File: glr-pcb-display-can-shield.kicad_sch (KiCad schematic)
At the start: 11 parts, among them CN12 Conn_02x08_Odd_Even, CN6 Conn_01x08, CN8 Conn_01x06, IC1 L9615D013TR, IC2 LF80CDT-TR, J1 Screw_Terminal_01x04, J2 Screw_Terminal_01x08

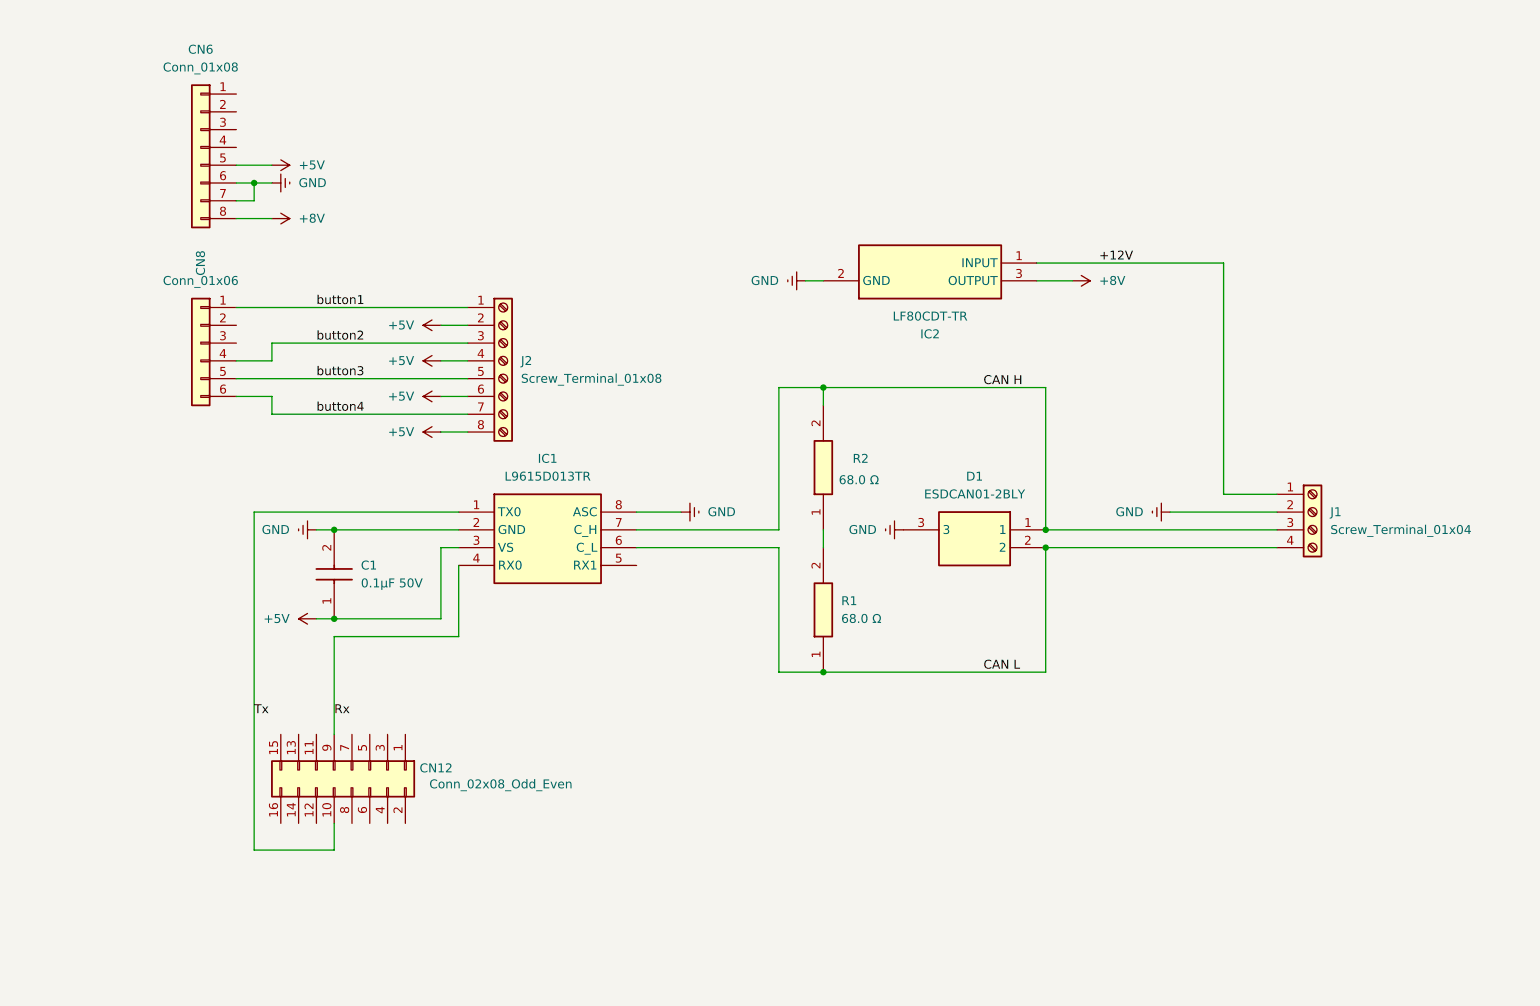
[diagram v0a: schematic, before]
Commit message: update can shield for new car
* provide more inputs for buttons and rotary encoders (not sure about that, big connector needed now)
* apply new can setup
* add new voltage transformer
* add full arduino headers
* m12a 4pin for power and can
* make board full size
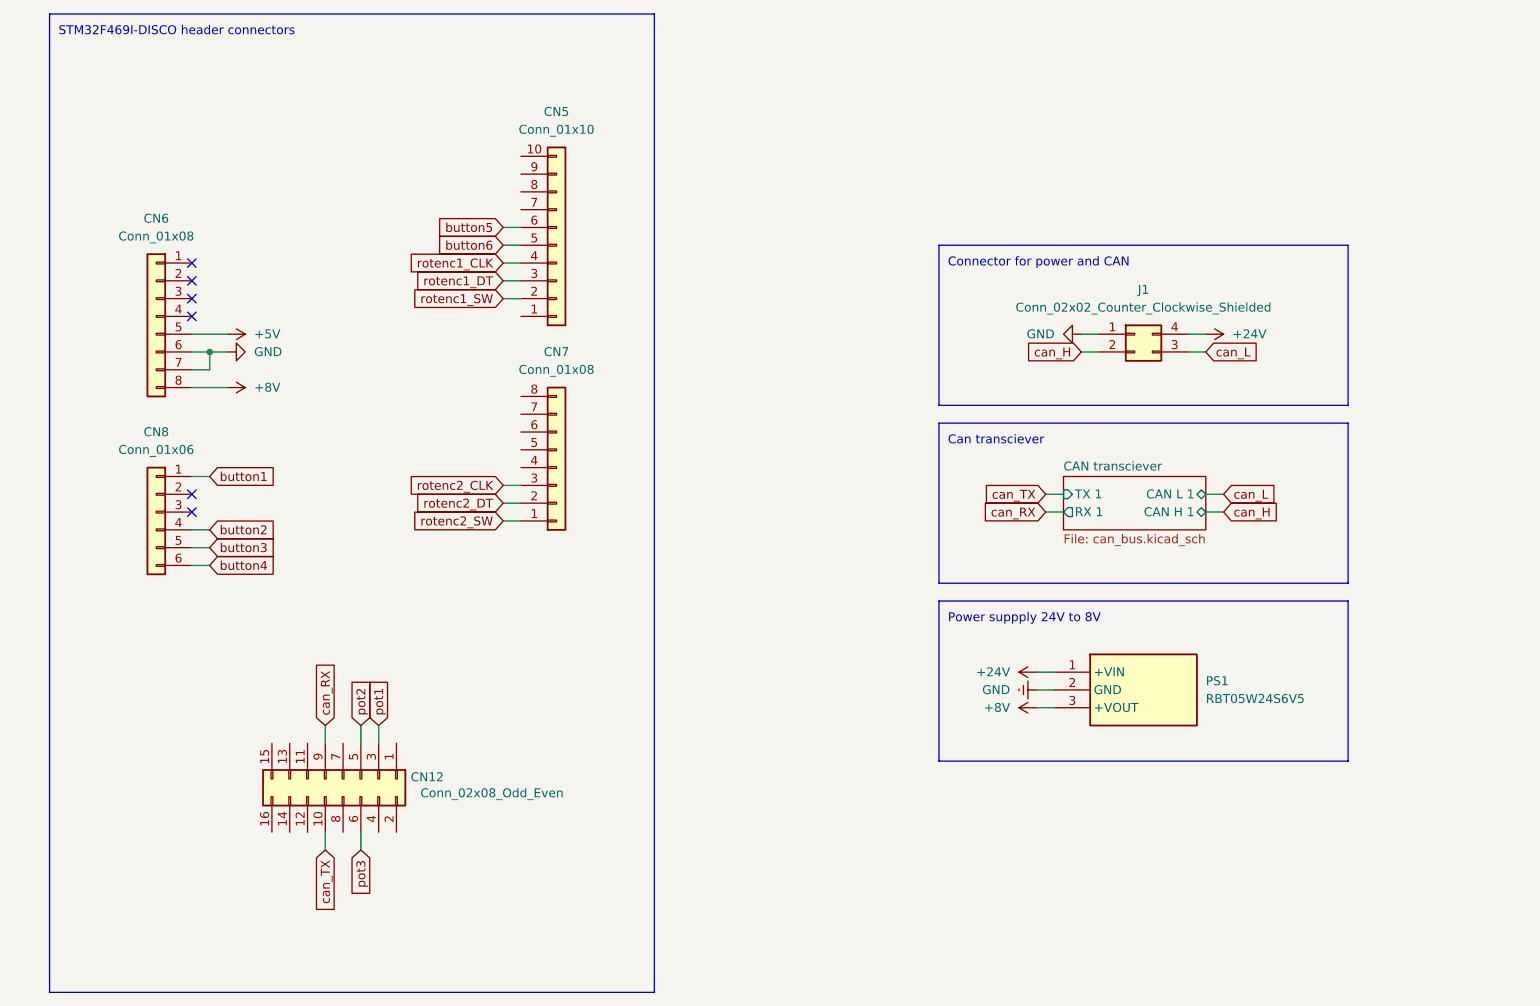
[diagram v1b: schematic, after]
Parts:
- removed C1: 0.1μF 50V, CAPC1608X90N, symbol SamacSys_Parts:CL10B104KB8NNNC
- removed D1: ESDCAN01-2BLY, SOT95P255X125-3N, symbol SamacSys_Parts:ESDCAN01-2BLY
- removed IC1: L9615D013TR, SOIC127P600X175-8N, symbol SamacSys_Parts:L9615D013TR
- removed IC2: LF80CDT-TR, LF80CDTTR, symbol SamacSys_Parts:LF80CDT-TR
- removed J1: Screw_Terminal_01x04, GLR_KiCAD_Library:WECO-950-FB-04, symbol Connector:Screw_Terminal_01x04
- removed J2: Screw_Terminal_01x08, GLR_KiCAD_Library:WECO-950-FB-08, symbol Connector:Screw_Terminal_01x08
- removed R1, R2: 68.0 Ω, RESC1608X50N, symbol SamacSys_Parts:CRCW060368R1FKEA
- added CN5: Conn_01x10, Connector_PinHeader_2.54mm:PinHeader_1x10_P2.54mm_Vertical, symbol Connector_Generic:Conn_01x10
- added CN7: Conn_01x08, Connector_PinHeader_2.54mm:PinHeader_1x08_P2.54mm_Vertical, symbol Connector_Generic:Conn_01x08
- added J1: Conn_02x02_Counter_Clockwise_Shielded, GLR_KiCad_Library:M12A-04P, symbol Connector_Generic:Conn_02x02_Counter_Clockwise
- added PS1: RBT05W24S6V5, RBT05W24S6V5, symbol SamacSys_Parts:RBT05W24S6V5
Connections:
- net +8V: now also PS1.3 (+VOUT)
- net GND: now also J1.1 (Pin_1), PS1.2 (GND)
- net pot1: now reaches CN12.3 (Pin_3)
- net pot2: now reaches CN12.5 (Pin_5)
- net pot3: now reaches CN12.6 (Pin_6)
- net Rx renamed can_RX
- net Tx renamed can_TX
- new net +24V: J1.4 (Pin_4), PS1.1 (+VIN)
- new net button5: CN5.6 (Pin_6)
- new net button6: CN5.5 (Pin_5)
- new net can_H: J1.2 (Pin_2)
- new net can_L: J1.3 (Pin_3)
- new net rotenc1_CLK: CN5.4 (Pin_4)
- new net rotenc1_DT: CN5.3 (Pin_3)
- new net rotenc1_SW: CN5.2 (Pin_2)
- new net rotenc2_CLK: CN7.3 (Pin_3)
- new net rotenc2_DT: CN7.2 (Pin_2)
- new net rotenc2_SW: CN7.1 (Pin_1)
- no-connect marks 0 -> 6
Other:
- added sheet CAN transciever (can_bus.kicad_sch)
- note added: "Can transciever"
- note added: "Connector for power and CAN"
- note added: "Power suppply 24V to 8V"
- note added: "STM32F469I-DISCO header connectors"
- moved on the sheet: CN12, CN6, CN8

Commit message: use absolute rotary encoders
* use more pins add dsub connector
* add documents
* routing should be done
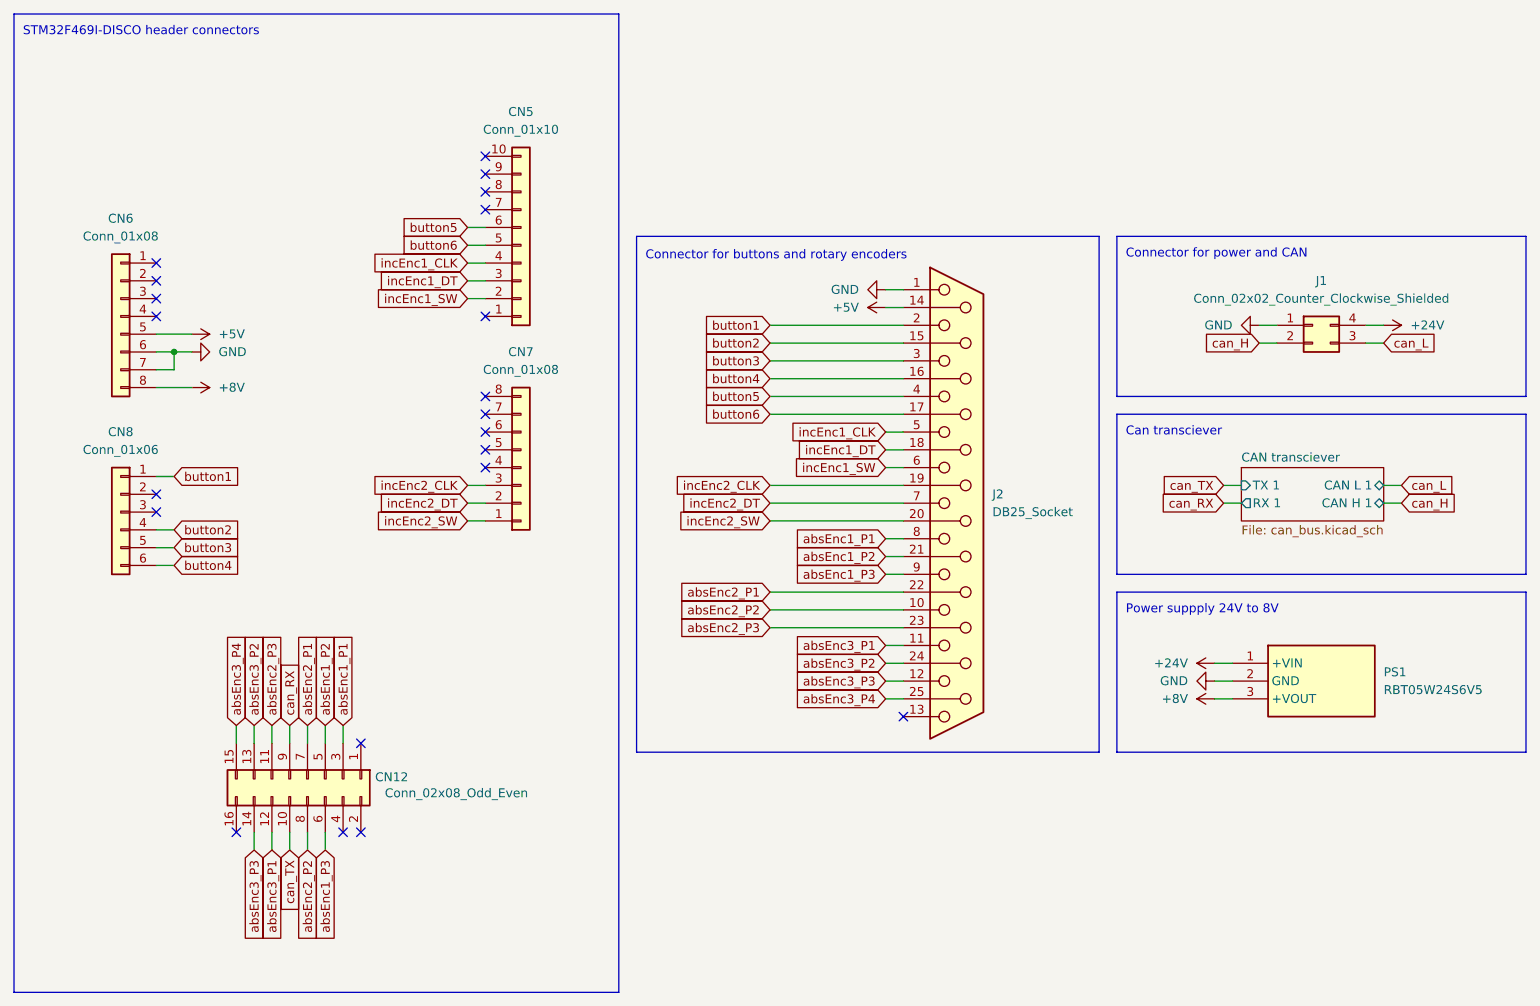
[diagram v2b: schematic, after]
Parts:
- added J2: DB25_Socket, Connector_Dsub:DSUB-25_Socket_Vertical_P2.77x2.84mm, symbol Connector:DB25_Socket
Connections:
- net +5V: now also J2.14 (P14)
- net GND: now also J2.1
- net button1: now also J2.2
- net button2: now also J2.15 (P15)
- net button3: now also J2.3
- net button4: now also J2.16 (P16)
- net button5: now also J2.4
- net button6: now also J2.17 (P17)
- net absEnc2_P3: now reaches CN12.11 (Pin_11)
- net absEnc2_P3: now also J2.23 (P23)
- net absEnc3_P1: now reaches CN12.12 (Pin_12)
- net absEnc3_P1: now also J2.11
- net absEnc3_P2: now reaches CN12.13 (Pin_13)
- net absEnc3_P2: now also J2.24 (P24)
- net absEnc3_P3: now reaches CN12.14 (Pin_14)
- net absEnc3_P3: now also J2.12
- net absEnc3_P4: now reaches CN12.15 (Pin_15)
- net absEnc3_P4: now also J2.25 (P25)
- net absEnc2_P1: now reaches CN12.7 (Pin_7)
- net absEnc2_P1: now also J2.22 (P22)
- net absEnc2_P2: now reaches CN12.8 (Pin_8)
- net absEnc2_P2: now also J2.10
- net pot1 renamed absEnc1_P1
- net absEnc1_P1: now also J2.8
- net pot2 renamed absEnc1_P2
- net absEnc1_P2: now also J2.21 (P21)
- net pot3 renamed absEnc1_P3
- net absEnc1_P3: now also J2.9
- net rotenc1_CLK renamed incEnc1_CLK
- net incEnc1_CLK: now also J2.5
- net rotenc1_DT renamed incEnc1_DT
- net incEnc1_DT: now also J2.18 (P18)
- net rotenc1_SW renamed incEnc1_SW
- net incEnc1_SW: now also J2.6
- net rotenc2_CLK renamed incEnc2_CLK
- net incEnc2_CLK: now also J2.19 (P19)
- net rotenc2_DT renamed incEnc2_DT
- net incEnc2_DT: now also J2.7
- net rotenc2_SW renamed incEnc2_SW
- net incEnc2_SW: now also J2.20 (P20)
- no-connect marks 6 -> 21
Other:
- note added: "Connector for buttons and rotary encoders"
- moved on the sheet: CN12, CN5, CN6, CN7, CN8, J1, PS1

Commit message: setup as aisler project
* update glr library
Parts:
- PS1: footprint RBT05W24S6V5 -> SamacSys_Parts:RBT05W24S6V5
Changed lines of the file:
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@@
 			)
 		)
-		(property "Footprint" "RBT05W24S6V5"
+		(property "Footprint" "SamacSys_Parts:RBT05W24S6V5"
 			(at 238.76 221.92 0)
 			(hide yes)

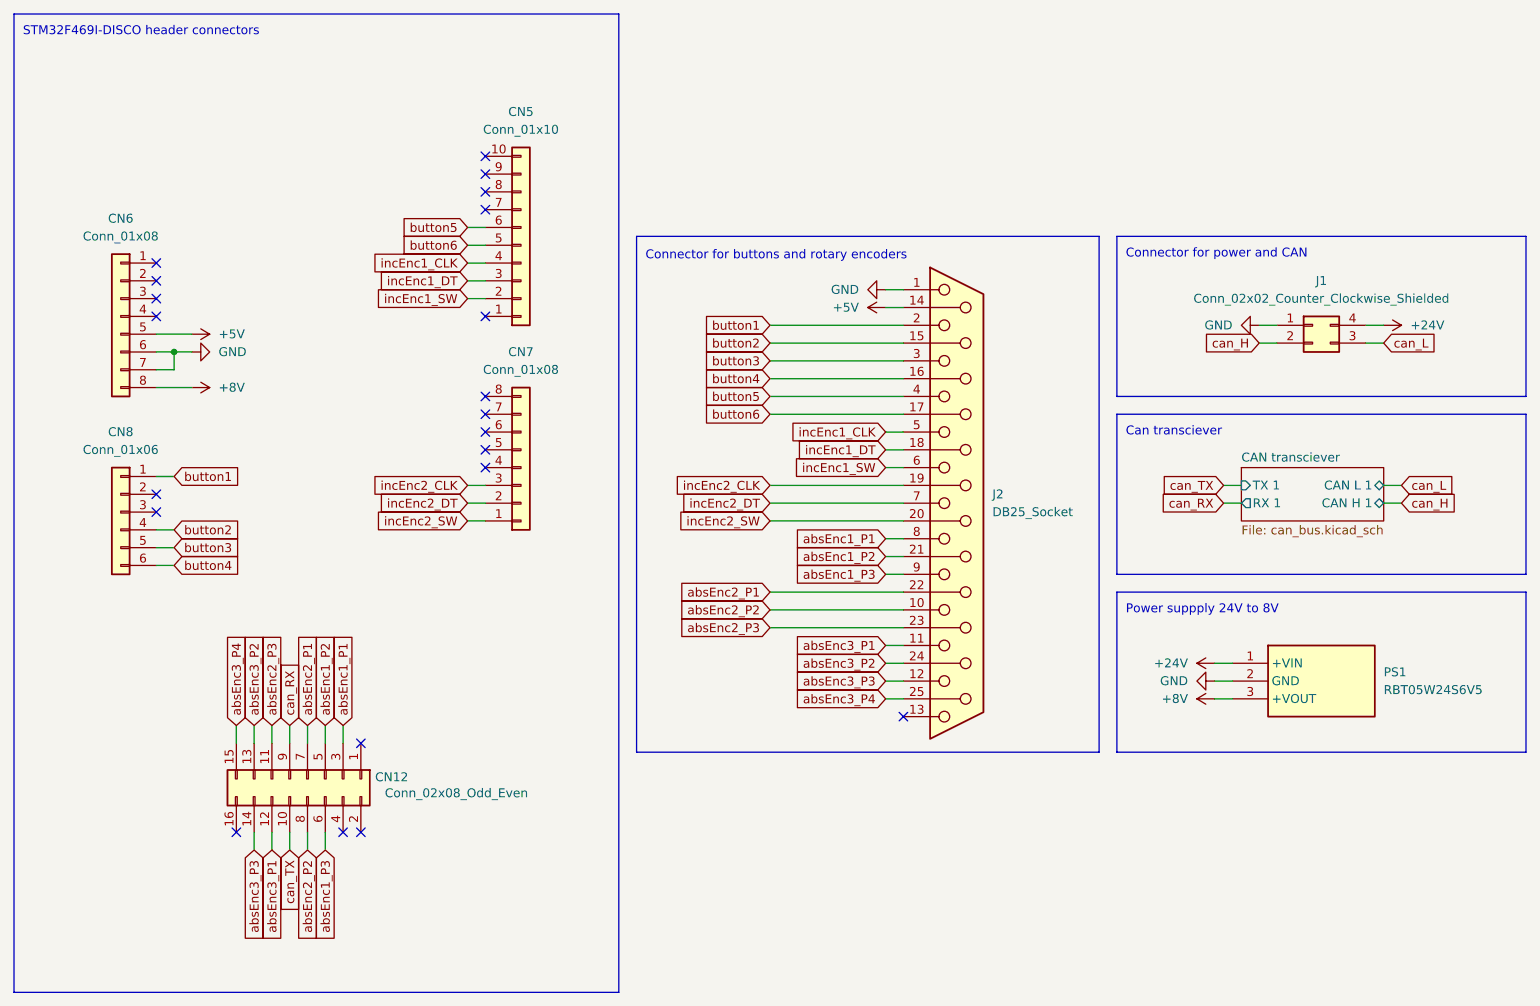
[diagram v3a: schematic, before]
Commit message: replace voltage regulator with buck converter
*
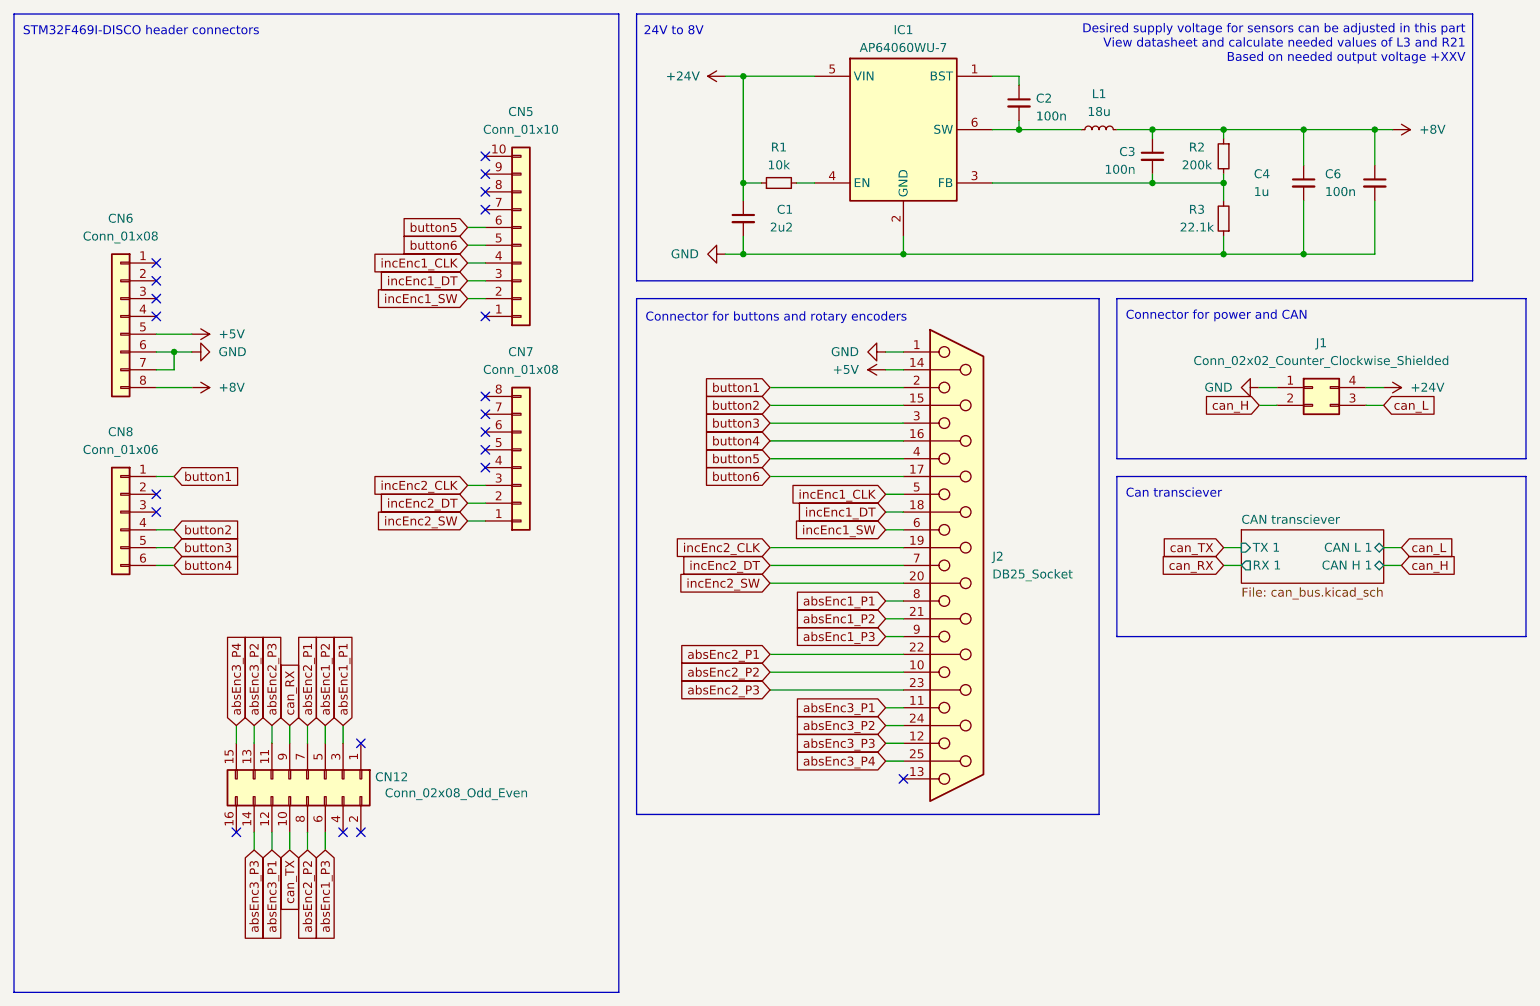
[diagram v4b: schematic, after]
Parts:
- removed PS1: RBT05W24S6V5, SamacSys_Parts:RBT05W24S6V5, symbol SamacSys_Parts:RBT05W24S6V5
- added C1: 2u2, Capacitor_SMD:C_0603_1608Metric, symbol Device:C_Small
- added C2, C3, C6: 100n, Capacitor_SMD:C_0603_1608Metric, symbol Device:C_Small
- added C4: 1u, Capacitor_SMD:C_0603_1608Metric, symbol Device:C_Small
- added IC1: AP64060WU-7, SamacSys_Parts:SOT95P280X100-6N, symbol SamacSys_Parts:AP64060WU-7
- added L1: 18u, Inductor_SMD:L_1008_2520Metric, symbol Device:L_Small
- added R1: 10k, Resistor_SMD:R_0603_1608Metric, symbol Device:R_Small
- added R2: 200k, Resistor_SMD:R_0603_1608Metric, symbol Device:R_Small
- added R3: 22.1k, Resistor_SMD:R_0603_1608Metric, symbol Device:R_Small
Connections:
- net +24V: now also C1.1, IC1.5 (VIN), R1.1
- net +8V: now also C3.1, C4.1, C6.1, L1.2, R2.1
- net GND: now also C1.2, C4.2, C6.2, IC1.2 (GND), R3.1
- new net: C3.2, IC1.3 (FB), R2.2, R3.2
- new net: IC1.4 (EN), R1.2
- new net: C2.1, IC1.1 (BST)
- new net: C2.2, IC1.6 (SW), L1.1
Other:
- note added: "24V to 8V"
- note added: "Desired supply voltage for sensors can be adjusted in this part View datasheet and calculate needed values of L3 and R21 Based on needed output voltage +XXV"
- note removed: "Power suppply 24V to 8V"
- moved on the sheet: J1, J2
